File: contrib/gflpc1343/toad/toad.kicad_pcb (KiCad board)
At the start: 4 copper layers, 84 x 82 mm, 241 parts, among them J1 RJ45, P1 GOODFET, P2 CPLD_JTAG, P3 TARGET5-8, P4 EXPANSION, P5 TARGET1-4, Q1 MOSFET_P, U1 UMN1N, U10 DG408, U11 GSG-LM339, U12 GSG-LM339, U13 GSG-LM339, U14 GSG-LM339, U15 UMP1N, U16 UMP1N, U17 MC4558, U18 GSG-MC34063, U19 MC4558, U2 UMN1N, U20 GSG-MC34063, U21 BH2228FV, U22 MC4558, U23 DG409, U24 DG409, U25 DG409, U26 AP7313, U27 DG409, U28 5M80ZT100, U29 GSG-AD5290, U3 DG408, U30 DG409, U31 MC4558, U4 DG408, U5 DG408, U6 DG408, U7 DG408, U8 DG408, U9 DG408

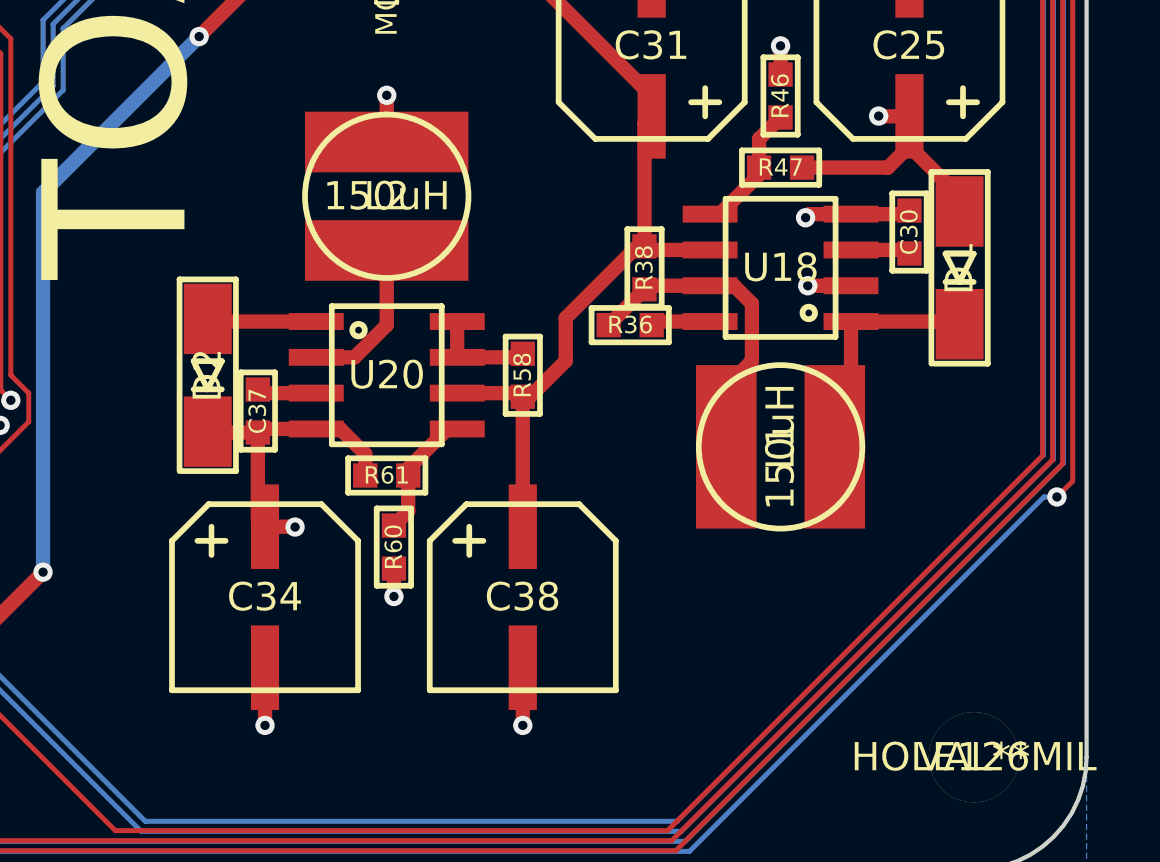
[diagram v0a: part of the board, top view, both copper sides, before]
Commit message: Resolved V+/V- issues by inverting D1, D2, C34 and changing U20 to voltage inverting configuration.
This is a manual edit, for fun and to be diff-friendly.  But it may have errors.


git-svn-id: https://svn.code.sf.net/p/goodfet/code@1663 12e2690d-a6be-4b82-a7b7-67c4a43b65c8
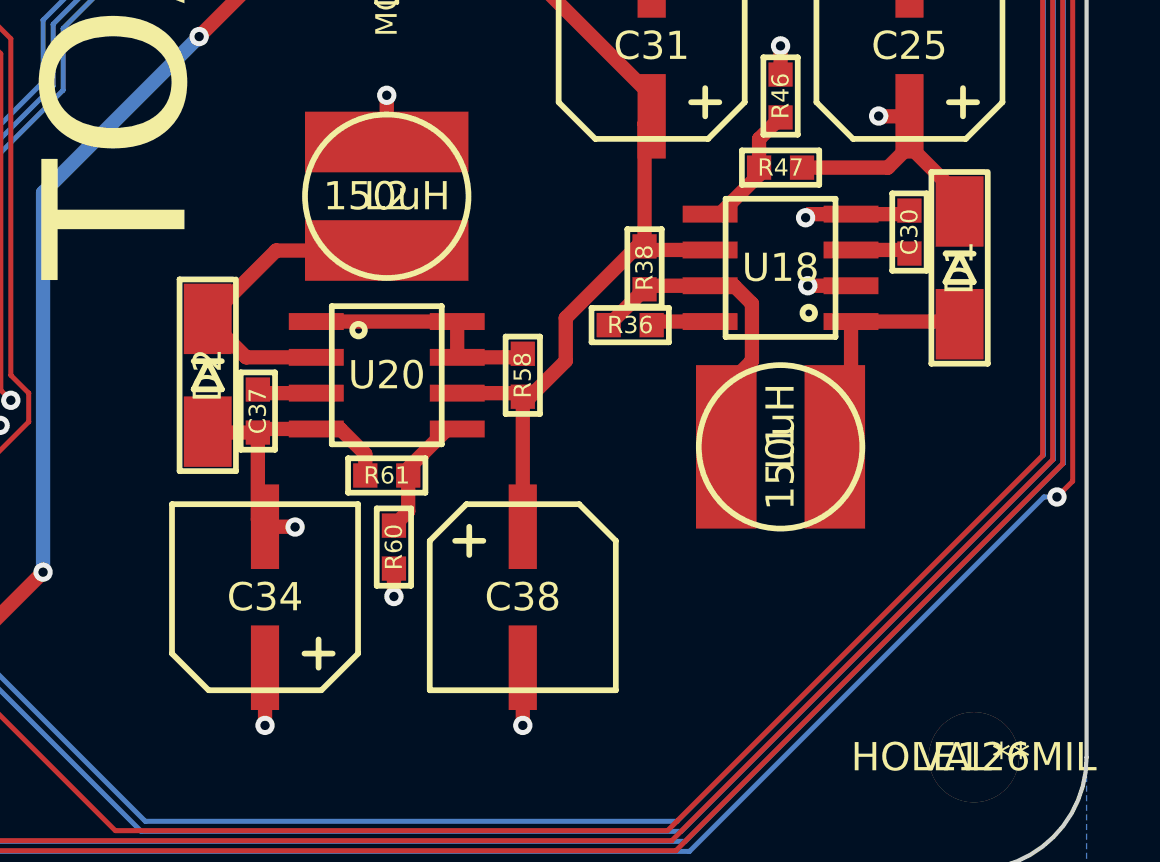
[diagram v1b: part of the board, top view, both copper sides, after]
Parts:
- turned C34 to 180 degrees
- turned D1 to 270 degrees
- turned D2 to 270 degrees
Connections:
- C34 pad 1: V- -> GND
- C34 pad 2: GND -> V-
- D1 pad 1: N-00000169 -> V+
- D1 pad 2: V+ -> N-00000169
- D2 pad 1: V- -> N-00000160
- D2 pad 2: N-00000158 -> V-
- U20 pad 1: N-00000158 -> N-00000152
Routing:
- net N-00000160: track 5.62 -> 11.8 mm
- net N-00000152: track 3.65 -> 8.65 mm
- net N-00000158: track 3.89 -> 0.00 mm
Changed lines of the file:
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@@
   (page A3)
   (layers
-    (15 F.Cu signal hide)
+    (15 F.Cu signal)
     (2 L2.Cu signal hide)
     (1 L3.Cu signal hide)
-    (0 B.Cu signal)
+    (0 B.Cu signal hide)
     (16 B.Adhes user)
     (17 F.Adhes user)
@@
     (pad_to_paste_clearance_ratio -0.12)
     (aux_axis_origin 0 0)
-    (visible_elements FFFF3FFF)
+    (visible_elements FFFD7FFF)
     (pcbplotparams
       (layerselection 283672583)
@@
   )
   (module GSG-UWT1V101MCL1GS   placed (layer F.Cu)
-    (at 130.556 166.624)
+    (at 130.556 166.624 180)
     (fp_text reference C34 (at 0 0) (layer F.SilkS)
       (effects (font (size 1.00076 1.00076) (thickness 0.2032)))
@@
     (pad 1 smd rect (at 0 -2.5) (size 1 3)
       (layers F.Cu F.Paste F.Mask)
-      (net 206 V-)
-      (die_length 0.2667)
+      (net 38 GND)
+      (die_length 0.12446)
     )
     (pad 2 smd rect (at 0 2.5) (size 1 3)
       (layers F.Cu F.Paste F.Mask)
-      (net 38 GND)
-      (die_length 0.12446)
+      (net 206 V-)
+      (die_length 0.2667)
     )
   )
@@
   )
   (module GSG-B140-13-F   placed (layer F.Cu)
-    (at 128.524 158.75 90)
+    (at 128.524 158.75 270)
     (fp_text reference D2 (at 0 0 90) (layer F.SilkS)
       (effects (font (size 1 1) (thickness 0.15)))
@@
     (pad 1 smd rect (at -2 0 90) (size 2.5 1.7)
       (layers F.Cu F.Paste F.Mask)
-      (net 206 V-)
+      (net 82 N-00000160)
     )
     (pad 2 smd rect (at 2 0 90) (size 2.5 1.7)
       (layers F.Cu F.Paste F.Mask)
-      (net 81 N-00000158)
+      (net 206 V-)
     )
   )
   (module GSG-B140-13-F   placed (layer F.Cu)
-    (at 155.194 154.94 90)
+    (at 155.194 154.94 270)
     (fp_text reference D1 (at 0 0 90) (layer F.SilkS)
       (effects (font (size 1 1) (thickness 0.15)))
@@
     (pad 1 smd rect (at -2 0 90) (size 2.5 1.7)
       (layers F.Cu F.Paste F.Mask)
-      (net 85 N-00000169)
+      (net 205 V+)
     )
     (pad 2 smd rect (at 2 0 90) (size 2.5 1.7)
       (layers F.Cu F.Paste F.Mask)
-      (net 205 V+)
+      (net 85 N-00000169)
     )
   )
@@
     (pad 1 smd rect (at -2.5 -1.905) (size 1.95 0.6)
       (layers F.Cu F.Paste F.Mask)
-      (net 81 N-00000158)
+      (net 78 N-00000152)
     )
     (pad 2 smd rect (at -2.5 -0.635) (size 1.95 0.6)
@@
   (segment (start 132.374 159.385) (end 130.429 159.385) (width 0.508) (layer F.Cu) (net 77) (status 30))
   (segment (start 130.429 159.385) (end 130.302 159.258) (width 0.508) (layer F.Cu) (net 77) (status 30))
+  (segment (start 137.374 156.845) (end 132.374 156.845) (width 0.508) (layer F.Cu) (net 78) (status 30))
   (segment (start 137.374 158.115) (end 137.374 156.845) (width 0.508) (layer F.Cu) (net 78) (status 30))
   (segment (start 137.374 158.115) (end 139.573 158.115) (width 0.508) (layer F.Cu) (net 78) (status 30))
@@
   (segment (start 85.2678 165.4556) (end 85.2678 166.3446) (width 0.1778) (layer F.Cu) (net 80))
   (segment (start 86.106 164.6174) (end 85.2678 165.4556) (width 0.1778) (layer F.Cu) (net 80) (status 10))
-  (segment (start 132.374 156.845) (end 128.619 156.845) (width 0.508) (layer F.Cu) (net 81) (status 30))
-  (segment (start 128.619 156.845) (end 128.524 156.75) (width 0.508) (layer F.Cu) (net 81) (status 30))
-  (segment (start 132.374 158.115) (end 133.731 158.115) (width 0.508) (layer F.Cu) (net 82) (status 10))
-  (segment (start 134.874 156.972) (end 134.874 154.325) (width 0.508) (layer F.Cu) (net 82) (status 20))
-  (segment (start 133.731 158.115) (end 134.874 156.972) (width 0.508) (layer F.Cu) (net 82))
+  (segment (start 134.874 154.325) (end 130.949 154.325) (width 0.508) (layer F.Cu) (net 82) (status 30))
+  (segment (start 130.949 154.325) (end 128.524 156.75) (width 0.508) (layer F.Cu) (net 82) (status 30))
+  (segment (start 132.374 158.115) (end 129.889 158.115) (width 0.508) (layer F.Cu) (net 82) (status 30))
+  (segment (start 129.889 158.115) (end 128.524 156.75) (width 0.508) (layer F.Cu) (net 82) (status 30))
   (segment (start 148.082 151.384) (end 148.082 150.368) (width 0.508) (layer F.Cu) (net 83) (status 10))
   (segment (start 148.082 150.368) (end 148.844 149.606) (width 0.508) (layer F.Cu) (net 83) (status 20))
